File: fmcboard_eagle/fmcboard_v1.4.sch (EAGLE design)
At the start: 146 parts, among them IC1 OPA699ID, IC10 LTC6229IMS8E#TRPBF, IC11 7805TV, IC12 SN74AUC2G66DCTR, IC13 SN74AUC2G66DCTR, IC14 SN74AUC2G66DCTR, IC15 SN74AUC2G66DCTR, IC16 DAC7578SPWR, IC2 DAC7578SPWR, IC3 LTC6229IMS8E#TRPBF, IC4 LTC6229IMS8E#TRPBF, IC5 LM358, IC6 OPA699ID, IC7 OPA699ID, IC8 LTC6229IMS8E#TRPBF, IC9 LTC6229IMS8E#TRPBF, J1 8pin, J10 8pin, J12 4p-2.54, J2 ASP-134604-01, J3 4p-2.54, J4 4p-2.54, J5 8pin, J6 4p-2.54, J7 4p-2.54, J8 4p-2.54, J9 8pin, U1 TXS0108EPWR, U2 STMICROELECTRONICS_L7905ACVST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

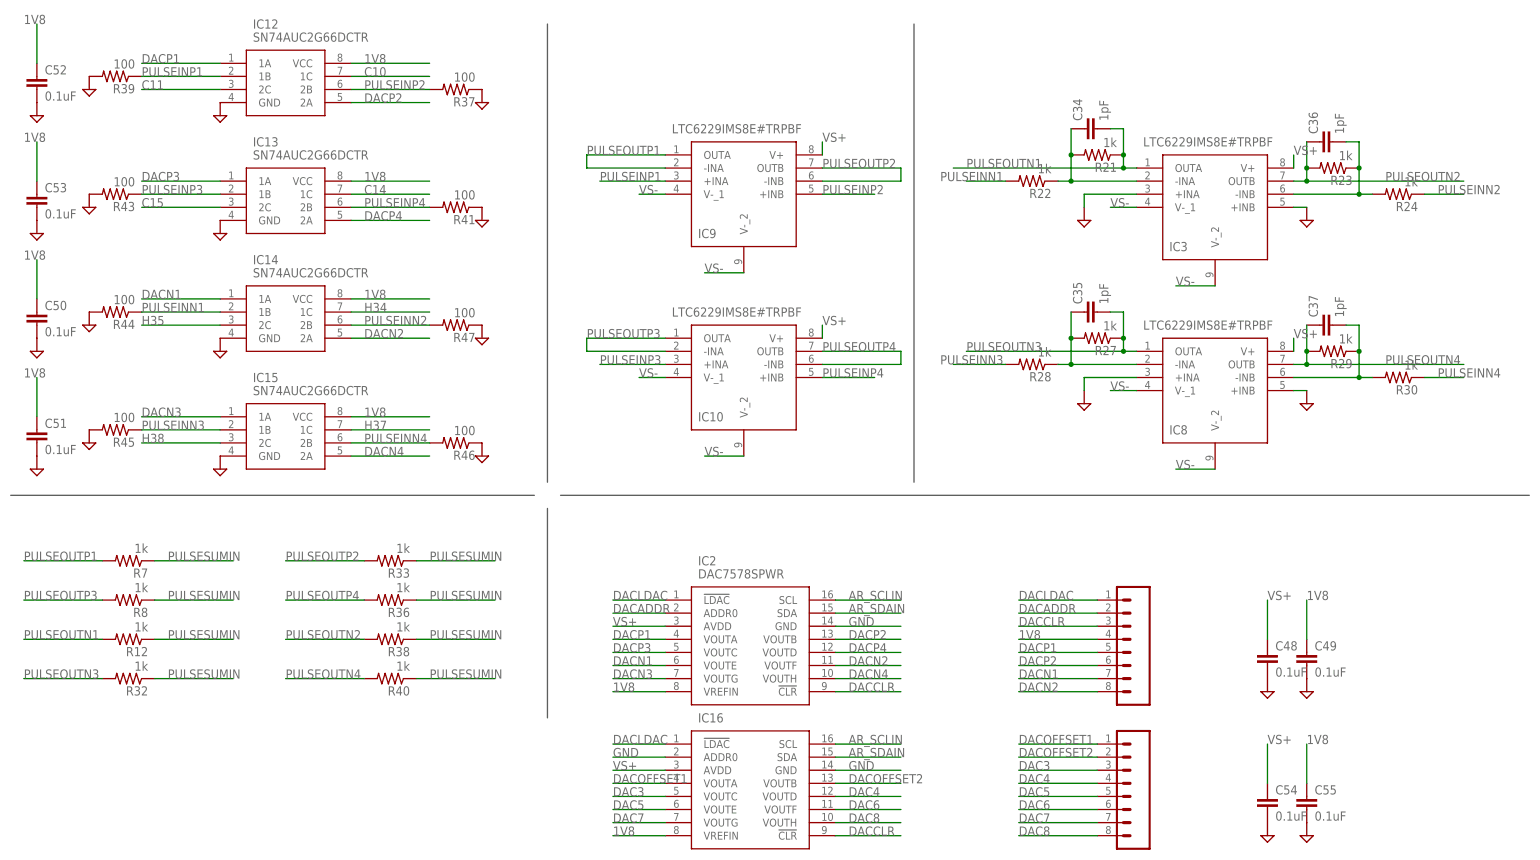
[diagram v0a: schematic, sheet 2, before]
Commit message: 1.43 add caps on dac outs
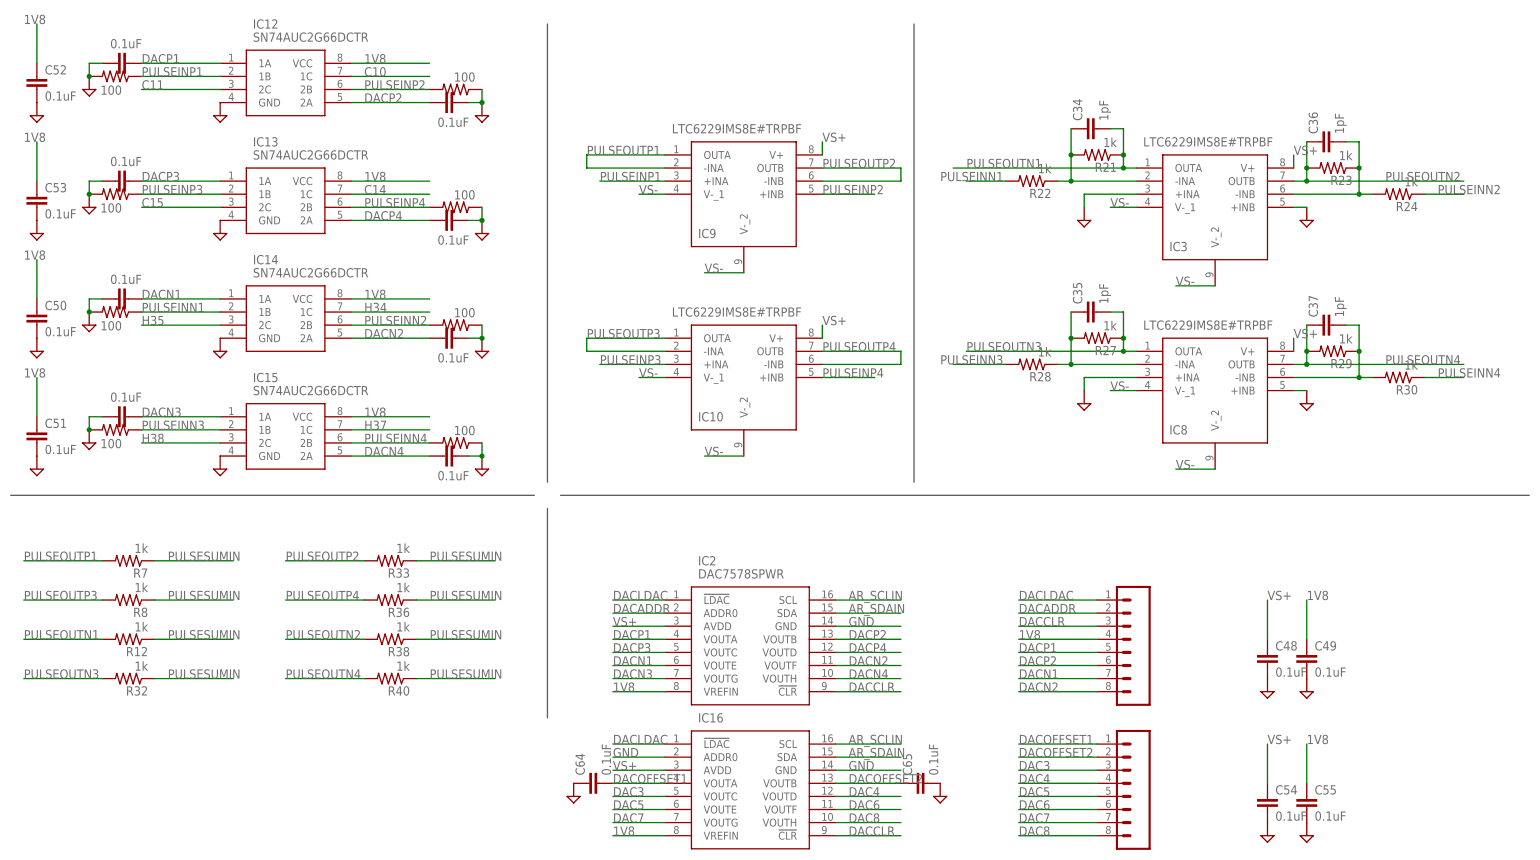
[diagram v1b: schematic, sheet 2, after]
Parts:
- added C56, C57, C58, C59, C60, C61, C62, C63, C64, C65: 0.1uF, SparkFun-Passives:CAP0805
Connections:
- net DACN1: now also C57.2
- net DACN2: now also C61.1
- net DACN3: now also C59.2
- net DACN4: now also C60.1
- net DACOFFSET1: now also C64.2
- net DACOFFSET2: now also C65.1
- net DACP1: now also C58.2
- net DACP2: now also C63.1
- net DACP3: now also C56.2
- net DACP4: now also C62.1
- net GND: now also C56.1, C57.1, C58.1, C59.1, C60.2, C61.2, C62.2, C63.2, C64.1, C65.2

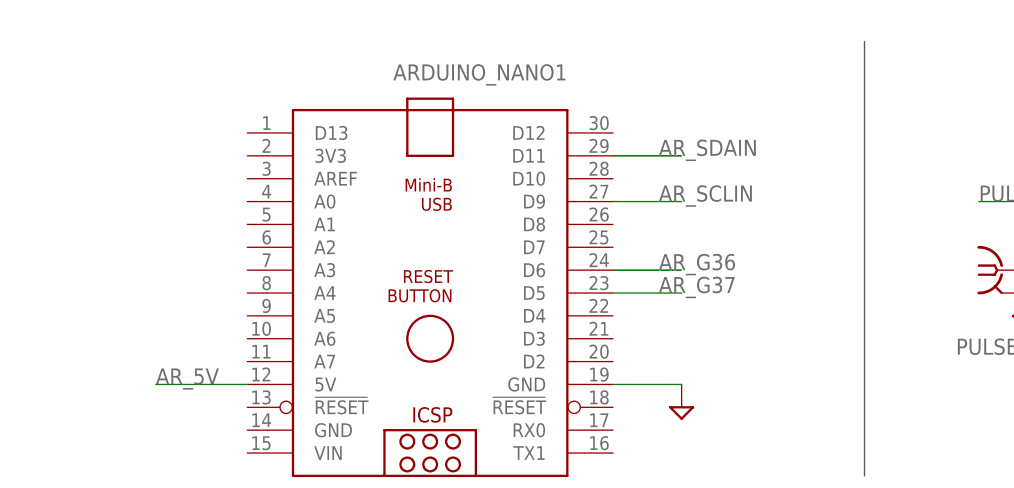
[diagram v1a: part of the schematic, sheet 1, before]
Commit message: 1.43 switch SDA and SCL for DACs to A4/5, add 4.7k pullups on SDA/SCL lines
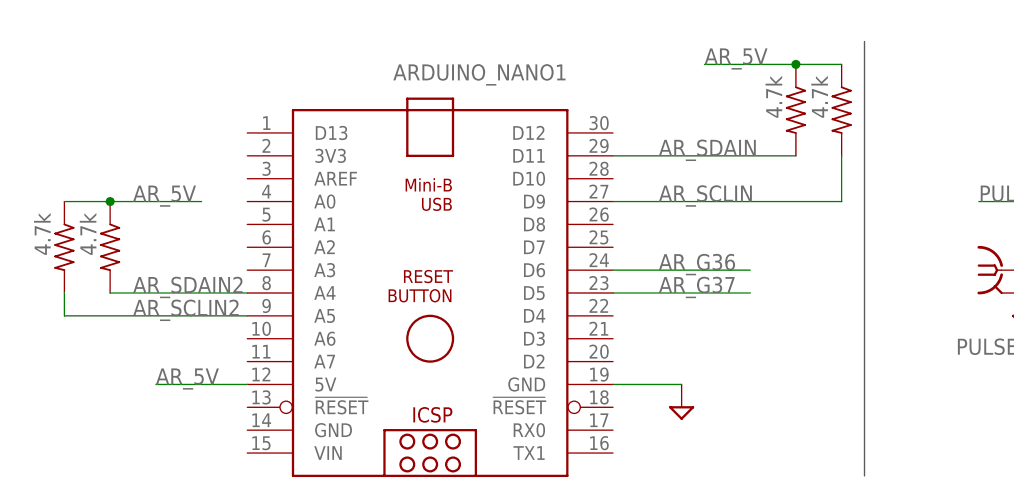
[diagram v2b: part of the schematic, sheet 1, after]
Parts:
- added R48, R49, R50, R51: 4.7k, rcl:R-US_R0805
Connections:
- new net AR_SCLIN2: ARDUINO_NANO1.A5, IC16.SCL, IC2.SCL, R49.2
- new net AR_SDAIN2: ARDUINO_NANO1.A4, IC16.SDA, IC2.SDA, R48.2
- net AR_5V: now also R48.1, R49.1, R50.1, R51.1
- net AR_SCLIN: now also R51.2; no longer IC16.SCL, IC2.SCL
- net AR_SDAIN: now also R50.2; no longer IC16.SDA, IC2.SDA
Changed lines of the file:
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@@
 <part name="SUPPLY75" library="supply2" library_urn="urn:adsk.eagle:library:372" deviceset="GND" device=""/>
 <part name="SUPPLY76" library="supply2" library_urn="urn:adsk.eagle:library:372" deviceset="GND" device=""/>
+<part name="R48" library="rcl" library_urn="urn:adsk.eagle:library:334" deviceset="R-US_" device="R0805" package3d_urn="urn:adsk.eagle:package:23553/2" value="4.7k"/>
+<part name="R49" library="rcl" library_urn="urn:adsk.eagle:library:334" deviceset="R-US_" device="R0805" package3d_urn="urn:adsk.eagle:package:23553/2" value="4.7k"/>
+<part name="R50" library="rcl" library_urn="urn:adsk.eagle:library:334" deviceset="R-US_" device="R0805" package3d_urn="urn:adsk.eagle:package:23553/2" value="4.7k"/>
+<part name="R51" library="rcl" library_urn="urn:adsk.eagle:library:334" deviceset="R-US_" device="R0805" package3d_urn="urn:adsk.eagle:package:23553/2" value="4.7k"/>
 </parts>
 <sheets>
@@
 </instance>
 <instance part="U2" gate="G$0" x="30.48" y="2.54" smashed="yes" rot="MR180"/>
+<instance part="R48" gate="G$1" x="-81.28" y="83.82" smashed="yes" rot="R270">
+<attribute name="VALUE" x="-84.582" y="87.63" size="1.778" layer="96" rot="R270"/>
+</instance>
+<instance part="R49" gate="G$1" x="-86.36" y="83.82" smashed="yes" rot="R270">
+<attribute name="VALUE" x="-89.662" y="87.63" size="1.778" layer="96" rot="R270"/>
+</instance>
+<instance part="R50" gate="G$1" x="-5.08" y="99.06" smashed="yes" rot="R270">
+<attribute name="VALUE" x="-8.382" y="102.87" size="1.778" layer="96" rot="R270"/>
+</instance>
+<instance part="R51" gate="G$1" x="0" y="99.06" smashed="yes" rot="R270">
+<attribute name="VALUE" x="-3.302" y="102.87" size="1.778" layer="96" rot="R270"/>
+</instance>
 </instances>
 <busses>
@@
 <net name="AR_SDAIN" class="0">
 <segment>
-<wire x1="-25.4" y1="93.98" x2="-17.78" y2="93.98" width="0.1524" layer="91"/>
+<wire x1="-25.4" y1="93.98" x2="-5.08" y2="93.98" width="0.1524" layer="91"/>
 <label x="-20.32" y="93.98" size="1.778" layer="95"/>
 <pinref part="ARDUINO_NANO1" gate="G$1" pin="D11"/>
+<pinref part="R50" gate="G$1" pin="2"/>
 </segment>
 <segment>
@@
 <net name="AR_SCLIN" class="0">
 <segment>
-<wire x1="-25.4" y1="88.9" x2="-17.78" y2="88.9" width="0.1524" layer="91"/>
+<wire x1="-25.4" y1="88.9" x2="0" y2="88.9" width="0.1524" layer="91"/>
 <label x="-20.32" y="88.9" size="1.778" layer="95"/>
 <pinref part="ARDUINO_NANO1" gate="G$1" pin="D9"/>
+<pinref part="R51" gate="G$1" pin="2"/>
+<wire x1="0" y1="93.98" x2="0" y2="88.9" width="0.1524" layer="91"/>
 </segment>
 <segment>
@@
 <segment>
 <pinref part="ARDUINO_NANO1" gate="G$1" pin="D6"/>
-<wire x1="-25.4" y1="81.28" x2="-17.78" y2="81.28" width="0.1524" layer="91"/>
+<wire x1="-25.4" y1="81.28" x2="-10.16" y2="81.28" width="0.1524" layer="91"/>
 <label x="-20.32" y="81.28" size="1.778" layer="95"/>
 </segment>
@@
 <segment>
 <pinref part="ARDUINO_NANO1" gate="G$1" pin="D5"/>
-<wire x1="-25.4" y1="78.74" x2="-17.78" y2="78.74" width="0.1524" layer="91"/>
+<wire x1="-25.4" y1="78.74" x2="-10.16" y2="78.74" width="0.1524" layer="91"/>
 <label x="-20.32" y="78.74" size="1.778" layer="95"/>
 </segment>
@@
 <wire x1="132.08" y1="38.1" x2="121.92" y2="38.1" width="0.1524" layer="91"/>
 <label x="121.92" y="38.1" size="1.778" layer="95"/>
+</segment>
+<segment>
+<pinref part="R49" gate="G$1" pin="1"/>
+<pinref part="R48" gate="G$1" pin="1"/>
+<wire x1="-86.36" y1="88.9" x2="-81.28" y2="88.9" width="0.1524" layer="91"/>
+<wire x1="-81.28" y1="88.9" x2="-71.12" y2="88.9" width="0.1524" layer="91"/>
+<junction x="-81.28" y="88.9"/>
+<label x="-78.74" y="88.9" size="1.778" layer="95"/>
+</segment>
+<segment>
+<pinref part="R51" gate="G$1" pin="1"/>
+<pinref part="R50" gate="G$1" pin="1"/>
+<wire x1="0" y1="104.14" x2="-5.08" y2="104.14" width="0.1524" layer="91"/>
+<wire x1="-5.08" y1="104.14" x2="-15.24" y2="104.14" width="0.1524" layer="91"/>
+<junction x="-5.08" y="104.14"/>
+<label x="-15.24" y="104.14" size="1.778" layer="95"/>
 </segment>
 </net>
@@
 <wire x1="132.08" y1="22.86" x2="121.92" y2="22.86" width="0.1524" layer="91"/>
 <label x="121.92" y="22.86" size="1.778" layer="95"/>
+</segment>
+</net>
+<net name="AR_SDAIN2" class="0">
+<segment>
+<pinref part="ARDUINO_NANO1" gate="G$1" pin="A4"/>
+<wire x1="-66.04" y1="78.74" x2="-81.28" y2="78.74" width="0.1524" layer="91"/>
+<label x="-78.74" y="78.74" size="1.778" layer="95"/>
+<pinref part="R48" gate="G$1" pin="2"/>
+</segment>
+</net>
+<net name="AR_SCLIN2" class="0">
+<segment>
+<pinref part="ARDUINO_NANO1" gate="G$1" pin="A5"/>
+<wire x1="-66.04" y1="76.2" x2="-86.36" y2="76.2" width="0.1524" layer="91"/>
+<label x="-78.74" y="76.2" size="1.778" layer="95"/>
+<pinref part="R49" gate="G$1" pin="2"/>
+<wire x1="-86.36" y1="76.2" x2="-86.36" y2="78.74" width="0.1524" layer="91"/>
 </segment>
 </net>
@@
 <attribute name="VALUE" x="98.044" y="99.441" size="1.778" layer="96"/>
 </instance>
-<instance part="C64" gate="G$1" x="129.54" y="-27.94" smashed="yes" rot="R90">
-<attribute name="NAME" x="126.619" y="-26.416" size="1.778" layer="95" rot="R90"/>
-<attribute name="VALUE" x="131.699" y="-26.416" size="1.778" layer="96" rot="R90"/>
-</instance>
-<instance part="C65" gate="G$1" x="193.04" y="-27.94" smashed="yes" rot="R90">
-<attribute name="NAME" x="190.119" y="-26.416" size="1.778" layer="95" rot="R90"/>
-<attribute name="VALUE" x="195.199" y="-26.416" size="1.778" layer="96" rot="R90"/>
-</instance>
-<instance part="SUPPLY75" gate="GND" x="124.46" y="-30.48" smashed="yes"/>
-<instance part="SUPPLY76" gate="GND" x="195.58" y="-30.48" smashed="yes"/>
+<instance part="C64" gate="G$1" x="124.46" y="-27.94" smashed="yes" rot="R90">
+<attribute name="VALUE" x="125.476" y="-23.241" size="1.778" layer="96" rot="R180"/>
+</instance>
+<instance part="C65" gate="G$1" x="198.12" y="-27.94" smashed="yes" rot="R90">
+<attribute name="VALUE" x="201.676" y="-23.241" size="1.778" layer="96" rot="R180"/>
+</instance>
+<instance part="SUPPLY75" gate="GND" x="119.38" y="-30.48" smashed="yes"/>
+<instance part="SUPPLY76" gate="GND" x="200.66" y="-30.48" smashed="yes"/>
 </instances>
 <busses>
@@
 </segment>
 </net>
-<net name="AR_SDAIN" class="0">
-<segment>
-<pinref part="IC2" gate="G$1" pin="SDA"/>
-<wire x1="175.26" y1="5.08" x2="187.96" y2="5.08" width="0.1524" layer="91"/>
-<label x="177.8" y="5.08" size="1.778" layer="95"/>
-</segment>
-<segment>
-<pinref part="IC16" gate="G$1" pin="SDA"/>
-<wire x1="175.26" y1="-22.86" x2="187.96" y2="-22.86" width="0.1524" layer="91"/>
-<label x="177.8" y="-22.86" size="1.778" layer="95"/>
-</segment>
-</net>
-<net name="AR_SCLIN" class="0">
-<segment>
-<pinref part="IC2" gate="G$1" pin="SCL"/>
-<wire x1="175.26" y1="7.62" x2="187.96" y2="7.62" width="0.1524" layer="91"/>
-<label x="177.8" y="7.62" size="1.778" layer="95"/>
-</segment>
-<segment>
-<pinref part="IC16" gate="G$1" pin="SCL"/>
-<wire x1="175.26" y1="-20.32" x2="187.96" y2="-20.32" width="0.1524" layer="91"/>
-<label x="177.8" y="-20.32" size="1.778" layer="95"/>
-</segment>
-</net>
 <net name="DACP2" class="0">
 <segment>
@@
 <segment>
 <pinref part="IC16" gate="G$1" pin="VOUTA"/>
-<wire x1="142.24" y1="-27.94" x2="132.08" y2="-27.94" width="0.1524" layer="91"/>
-<label x="132.08" y="-27.94" size="1.778" layer="95"/>
+<wire x1="142.24" y1="-27.94" x2="127" y2="-27.94" width="0.1524" layer="91"/>
+<label x="127" y="-27.94" size="1.778" layer="95"/>
 <pinref part="C64" gate="G$1" pin="2"/>
 </segment>
@@
 <segment>
 <pinref part="IC16" gate="G$1" pin="VOUTB"/>
-<wire x1="175.26" y1="-27.94" x2="187.96" y2="-27.94" width="0.1524" layer="91"/>
+<wire x1="175.26" y1="-27.94" x2="193.04" y2="-27.94" width="0.1524" layer="91"/>
 <label x="177.8" y="-27.94" size="1.778" layer="95"/>
 <pinref part="C65" gate="G$1" pin="1"/>
@@
 </segment>
 </net>
+<net name="AR_SCLIN2" class="0">
+<segment>
+<pinref part="IC2" gate="G$1" pin="SCL"/>
+<wire x1="175.26" y1="7.62" x2="187.96" y2="7.62" width="0.1524" layer="91"/>
+<label x="177.8" y="7.62" size="1.778" layer="95"/>
+</segment>
+<segment>
+<pinref part="IC16" gate="G$1" pin="SCL"/>
+<wire x1="175.26" y1="-20.32" x2="187.96" y2="-20.32" width="0.1524" layer="91"/>
+<label x="177.8" y="-20.32" size="1.778" layer="95"/>
+</segment>
+</net>
+<net name="AR_SDAIN2" class="0">
+<segment>
+<pinref part="IC2" gate="G$1" pin="SDA"/>
+<wire x1="175.26" y1="5.08" x2="187.96" y2="5.08" width="0.1524" layer="91"/>
+<label x="177.8" y="5.08" size="1.778" layer="95"/>
+</segment>
+<segment>
+<pinref part="IC16" gate="G$1" pin="SDA"/>
+<wire x1="175.26" y1="-22.86" x2="187.96" y2="-22.86" width="0.1524" layer="91"/>
+<label x="177.8" y="-22.86" size="1.778" layer="95"/>
+</segment>
+</net>
